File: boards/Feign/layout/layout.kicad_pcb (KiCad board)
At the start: 4 copper layers, 34.2 x 16.3 mm, 33 parts, among them IC1 TPD4E05U06QDQARQ1, J1 M20-8890645R, J2 ?, J3 USB4105-GF-A, SW1 B3U-1000P, SW2 B3U-1000P, U1 TPS74501PDRVR, U2 STM32G0B1KBU6N, U3 TPS2553DRVR

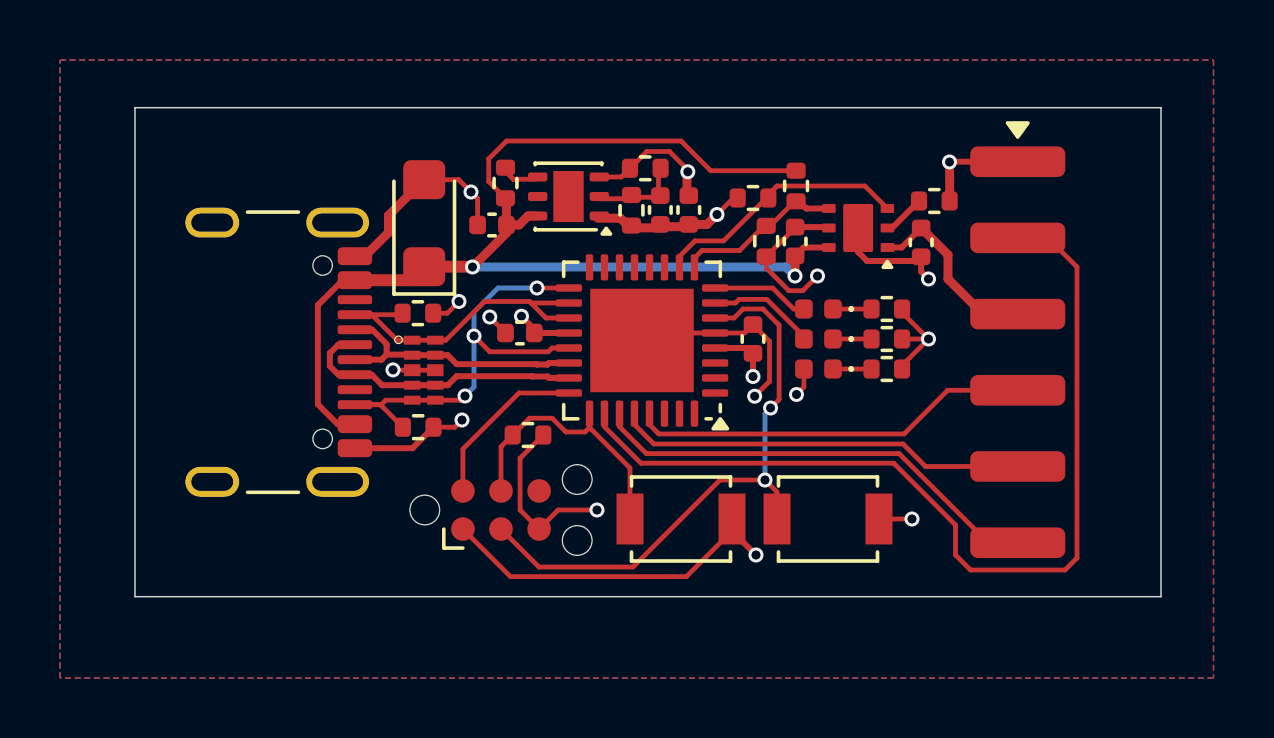
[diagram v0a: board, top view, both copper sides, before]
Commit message: feat(Feign): add 3 front-side fiducials
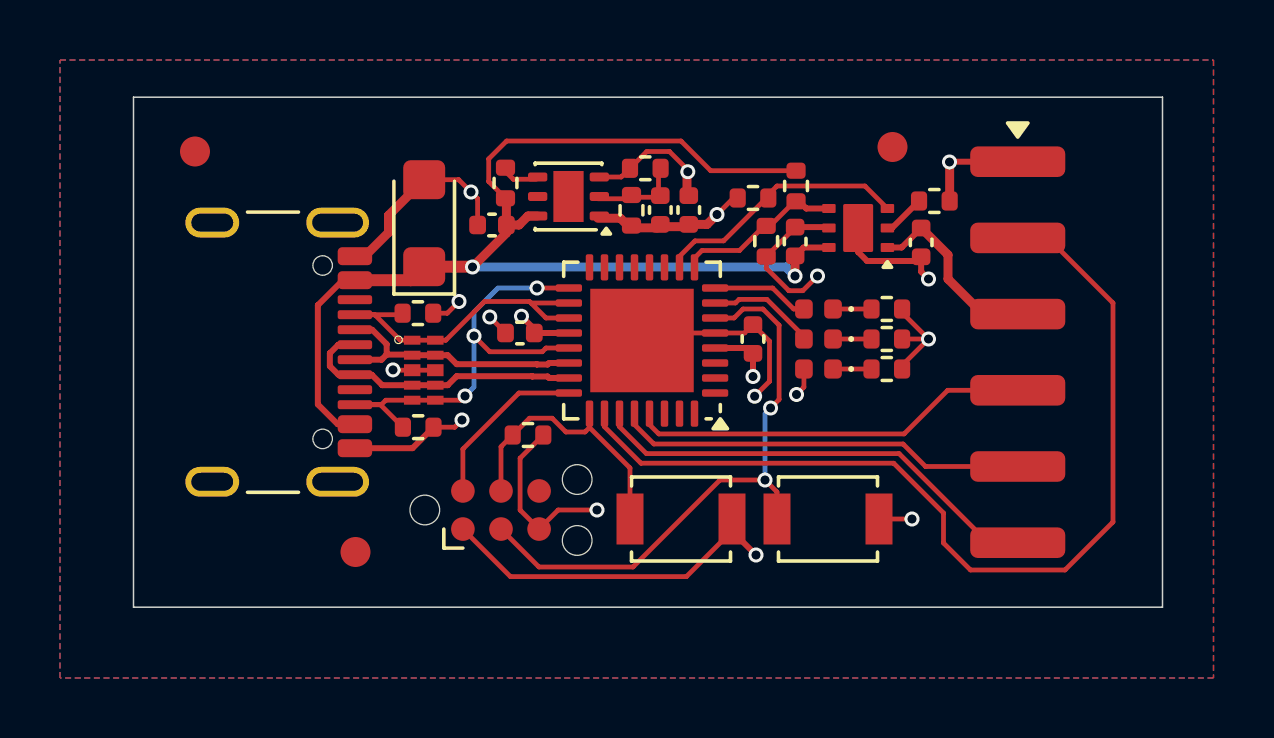
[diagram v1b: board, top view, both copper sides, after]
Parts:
- added FID1: Fiducial, kicad_libraries_kicad-footprints_Fiducial@9.0.3:Fiducial_1mm_Mask2mm, F.Cu at (127.1, 102.2)
- added FID2: Fiducial, kicad_libraries_kicad-footprints_Fiducial@9.0.3:Fiducial_1mm_Mask2mm, F.Cu at (150.3, 102.1)
- added FID3: Fiducial, kicad_libraries_kicad-footprints_Fiducial@9.0.3:Fiducial_1mm_Mask2mm, F.Cu at (132.4, 115.6)
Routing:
- net MODEM_CTS: track 31.0 -> 32.0 mm
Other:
- board size 34.2 x 16.3 mm -> 34.3 x 17 mm

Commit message: feat(Feign): add silkscreen version stamp and Diode logo
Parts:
- added #G1: ?, diodeinc_registry_modules_Logo@0.5.0:diode, B.Cu at (131.8, 109.0)
- added V1: ?, stdlib_generics_footprints:version-footprint, B.Cu at (142.0, 108.5)

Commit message: layout(Feign): swap inner planes \u2014 GND on In1, V3V3 on In2
USB diff pair on F.Cu now references the GND plane immediately below
instead of V3V3, per EE review (clean reference plane for return
current).
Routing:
- added copper zone on In1.Cu, net GND
- added copper zone on In2.Cu, net V3V3
- removed copper zone on In2.Cu, net GND
- removed copper zone on In1.Cu, net V3V3
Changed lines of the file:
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@@
 		(net 7)
 		(net_name "GND")
-		(layers "F.Cu" "B.Cu" "In2.Cu")
+		(layers "F.Cu" "B.Cu" "In1.Cu")
 		(hatch edge 0.5)
 		(connect_pads
@@
 		(net 2)
 		(net_name "V3V3")
-		(layer "In1.Cu")
+		(layer "In2.Cu")
 		(hatch edge 0.5)
 		(connect_pads
